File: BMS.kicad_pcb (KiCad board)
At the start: 2 copper layers, 44 parts, among them J28 OLED, SW14 SW_DIP_x01, SW15 SW_DIP_x01, SW16 SW_DIP_x01, U10 ISO1050DUB, U2 TSR_1-2450, U4 Teensy4.1, U6 TBA1-0511E, U7 ISO1050DUB, U8 ISO1050DUB, U9 ISO7221C

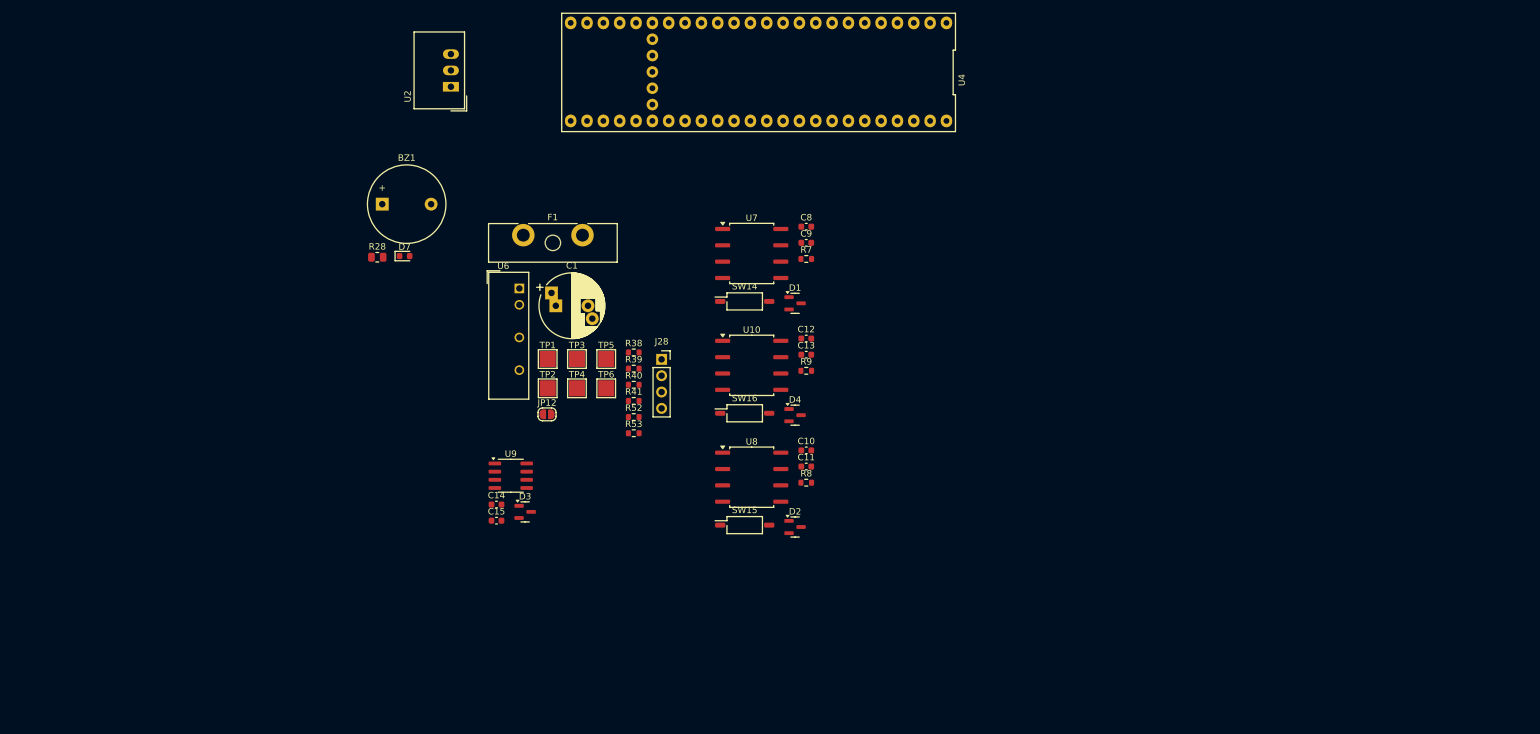
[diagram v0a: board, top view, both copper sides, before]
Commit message: Connectors, high side circuits added, layout progressed
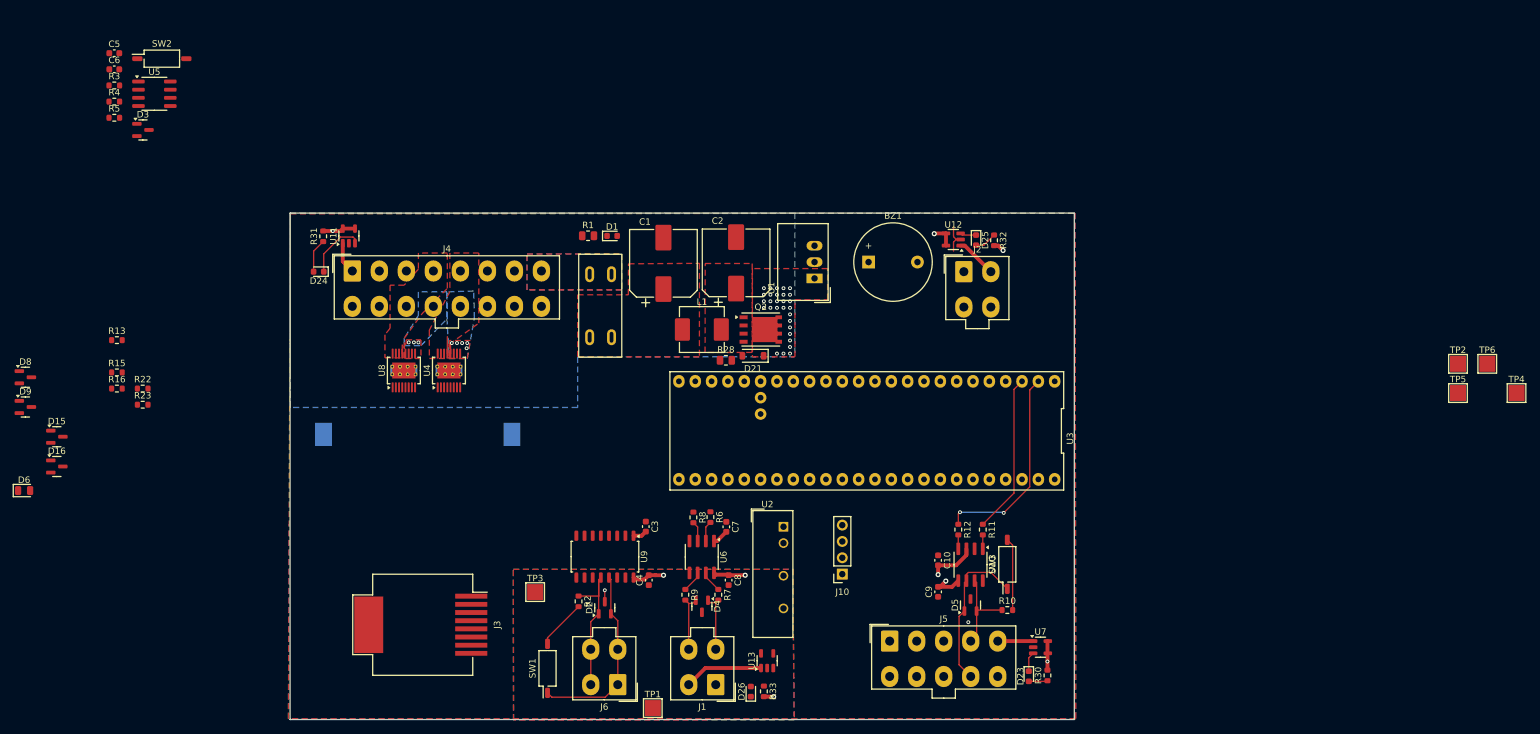
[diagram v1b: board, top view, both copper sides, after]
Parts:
- removed C11, C12, C13: 1uF, Capacitor_SMD:C_0603_1608Metric
- removed the D2 at (155.0, 117.9)
- removed the D4 at (155.0, 100.5)
- removed JP12: SolderJumper_2_Open, Jumper:SolderJumper-2_P1.3mm_Open_RoundedPad1.0x1.5mm
- removed R38, R39, R40, R41, R52, R53: 330R, Resistor_SMD:R_0603_1608Metric
- removed SW15, SW16: SW_DIP_x01, Button_Switch_SMD:SW_DIP_SPSTx01_Slide_Copal_CHS-01B_W7.62mm_P1.27mm
- added BT1: Battery_Cell, Battery:BatteryHolder_Keystone_1060_1x2032, B.Cu at (96.3, 103.5)
- added C2: 470uF, Capacitor_SMD:CP_Elec_10x10, F.Cu at (145.8, 76.8)
- added C5: 1uF, Capacitor_SMD:C_0603_1608Metric, F.Cu at (49.1, 44.2)
- added C6: 1uF, Capacitor_SMD:C_0603_1608Metric, F.Cu at (49.1, 46.7)
- added C9: 1uF, Capacitor_SMD:C_0603_1608Metric, F.Cu at (177.2, 128.0)
- added D15: BAT54S, Package_TO_SOT_SMD:SOT-23, F.Cu at (40.2, 103.9)
- added D16: BAT54S, Package_TO_SOT_SMD:SOT-23, F.Cu at (40.2, 108.5)
- added D21: 10V, Diode_SMD:D_SOD-123, F.Cu at (148.4, 91.3)
- added D23: LED_RED, LED_SMD:LED_0603_1608Metric, F.Cu at (191.3, 141.1)
- added D24: LED_RED, LED_SMD:LED_0603_1608Metric, F.Cu at (80.9, 78.2)
- added D25: LED_RED, LED_SMD:LED_0603_1608Metric, F.Cu at (183.1, 73.3)
- added D26: LED_RED, LED_SMD:LED_0603_1608Metric, F.Cu at (148.1, 143.5)
- added D3: PESD1CAN, Package_TO_SOT_SMD:SOT-23, F.Cu at (53.6, 56.2)
- added D5: PESD1CAN, Package_TO_SOT_SMD:SOT-23, F.Cu at (182.2, 130.0)
- added D6: D, Diode_SMD:D_0805_2012Metric, F.Cu at (35.1, 112.2)
- added D8: BAT54S, Package_TO_SOT_SMD:SOT-23, F.Cu at (35.3, 94.6)
- added D9: BAT54S, Package_TO_SOT_SMD:SOT-23, F.Cu at (35.3, 99.2)
- added J1: Conn_02x02_Counter_Clockwise, Connector_Molex:Molex_Mini-Fit_Jr_5566-04A_2x02_P4.20mm_Vertical, F.Cu at (142.6, 142.4)
- added J2: Conn_02x02_Counter_Clockwise, Connector_Molex:Molex_Mini-Fit_Jr_5566-04A_2x02_P4.20mm_Vertical, F.Cu at (181.2, 78.2)
- added J3: RJ45, Connector_RJ:RJ45_Molex_0855135013_Vertical, F.Cu at (96.8, 133.1)
- added J4: Conn_02x08_Top_Bottom, Connector_Molex:Molex_Mini-Fit_Jr_5566-16A_2x08_P4.20mm_Vertical, F.Cu at (86.1, 78.1)
- added J5: Conn_02x05_Top_Bottom, Connector_Molex:Molex_Mini-Fit_Jr_5566-10A_2x05_P4.20mm_Vertical, F.Cu at (169.7, 135.6)
- added J6: Conn_02x02_Counter_Clockwise, Connector_Molex:Molex_Mini-Fit_Jr_5566-04A_2x02_P4.20mm_Vertical, F.Cu at (127.4, 142.4)
- added L1: 1.5uH, Inductor_SMD:L_Changjiang_FXL0618, F.Cu at (140.5, 87.2)
- added Q2: SIRA00DP-T1-GE3, Package_SO:PowerPAK_SO-8_Single, F.Cu at (149.6, 87.2)
- added R10: 120, Resistor_SMD:R_0603_1608Metric, F.Cu at (188.0, 130.8)
- added R11: 330R, Resistor_SMD:R_0603_1608Metric, F.Cu at (184.2, 118.3)
- added R12: 330R, Resistor_SMD:R_0603_1608Metric, F.Cu at (180.3, 118.3)
- added R13: 4.7k, Resistor_SMD:R_0603_1608Metric, F.Cu at (49.5, 88.8)
- added R15: 15k, Resistor_SMD:R_0603_1608Metric, F.Cu at (49.5, 93.9)
- added R16: 15k, Resistor_SMD:R_0603_1608Metric, F.Cu at (49.5, 96.4)
- added R22: 15k, Resistor_SMD:R_0603_1608Metric, F.Cu at (53.5, 96.4)
- added R23: 15k, Resistor_SMD:R_0603_1608Metric, F.Cu at (53.5, 98.9)
- added R28: 10k, Resistor_SMD:R_0805_2012Metric, F.Cu at (144.2, 92.0)
- added R3: 120, Resistor_SMD:R_0603_1608Metric, F.Cu at (49.1, 49.3)
- added R30: 3.3k, Resistor_SMD:R_0603_1608Metric, F.Cu at (194.2, 141.0)
- added R31: 3.3k, Resistor_SMD:R_0603_1608Metric, F.Cu at (81.6, 72.7)
- added R32: 3.3k, Resistor_SMD:R_0603_1608Metric, F.Cu at (185.9, 73.3)
- added R33: 3.3k, Resistor_SMD:R_0603_1608Metric, F.Cu at (150.1, 143.4)
- added R4: 330R, Resistor_SMD:R_0603_1608Metric, F.Cu at (49.1, 51.8)
- added R5: 330R, Resistor_SMD:R_0603_1608Metric, F.Cu at (49.1, 54.3)
- added R6: 330R, Resistor_SMD:R_0603_1608Metric, F.Cu at (141.8, 116.4)
- added R7: 330R, Resistor_SMD:R_0603_1608Metric, F.Cu at (143.0, 128.4)
- added SW2: SW_DIP_x01, Button_Switch_SMD:SW_DIP_SPSTx01_Slide_Copal_CHS-01B_W7.62mm_P1.27mm, F.Cu at (56.5, 45.1)
- added SW3: SW_DIP_x01, Button_Switch_SMD:SW_DIP_SPSTx01_Slide_Copal_CHS-01B_W7.62mm_P1.27mm, F.Cu at (188.0, 123.7)
- added U11: TPS2051CDBV, Package_TO_SOT_SMD:SOT-23-5, F.Cu at (85.6, 72.6)
- added U12: TPS2051CDBV, Package_TO_SOT_SMD:SOT-23-5, F.Cu at (179.6, 73.2)
- added U13: TPS2051CDBV, Package_TO_SOT_SMD:SOT-23-5, F.Cu at (150.6, 138.7)
- added U4: VND7050AJTR, Package_SO:PowerSSO-16-1EP_3.9x4.9mm_P0.5mm_EP2.5x3.61mm_ThermalVias, F.Cu at (101.2, 93.6)
- added U5: TJA1051T/3/1J, Package_SO:SOIC-8_3.9x4.9mm_P1.27mm, F.Cu at (55.4, 50.5)
- added U9: ISO1050DWR, Package_SO:SOP-16_4.55x10.3mm_P1.27mm, F.Cu at (125.4, 122.5)
- C1: value 1000uf 50V -> 470uF; footprint Capacitor_THT:CP_Radial_D10.0mm_P5.00mm_P7.50mm -> Capacitor_SMD:CP_Elec_10x10
- F1: value 20A Fuse -> Mini Blade Fuse (10A); footprint Fuse:Fuseholder_Blade_ATO_Littelfuse_Pudenz_2_Pin -> user:XFCN XF-508P-B-B
- R8, R9: value 120 -> 330R
- U1: renamed from U2; value TSR_1-2450 -> K7805M-1000R3
- U10: value ISO1050DUB -> TJA1051T/3/1J; footprint Package_SO:SOP-8_6.62x9.15mm_P2.54mm -> Package_SO:SOIC-8_3.9x4.9mm_P1.27mm
- U2: renamed from U6; value TBA1-0511E -> B0505S-3WR2
- U6: renamed from U9; value ISO7221C -> ISO7331C
- U7: value ISO1050DUB -> TPS2051CDBV; footprint Package_SO:SOP-8_6.62x9.15mm_P2.54mm -> Package_TO_SOT_SMD:SOT-23-5
- U8: value ISO1050DUB -> VND7050AJTR; footprint Package_SO:SOP-8_6.62x9.15mm_P2.54mm -> Package_SO:PowerSSO-16-1EP_3.9x4.9mm_P0.5mm_EP2.5x3.61mm_ThermalVias
- moved TP2 141.5 mm to (258.0, 92.5)
- moved TP4 141.5 mm to (267.1, 97.1)
- moved TP5 141.5 mm to (258.0, 97.1)
- moved TP6 141.5 mm to (262.6, 92.5)
- moved BZ1 76.1 mm to (166.4, 76.7)
- moved U7 75.9 mm to (193.1, 136.6)
- moved SW1 64.8 mm to (116.5, 139.9), turned to 90 degrees
- moved R2 63.9 mm to (121.3, 129.5), turned to -90 degrees
- moved U1 63.9 mm to (158.0, 79.2)
- moved U3 58.2 mm to (166.1, 104.1)
- moved C4 57.9 mm to (132.2, 126.2), turned to 90 degrees
- moved U8 56.6 mm to (94.1, 93.6), turned to 90 degrees
- moved D2 55.8 mm to (125.4, 130.5), turned to 90 degrees
- moved U2 55.3 mm to (153.2, 117.9)
- moved TP1 54.7 mm to (132.8, 146.1)
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- renumbered C8 to C3, C9 to C4, C14 to C7, C15 to C8, D7 to D1, D1 to D2, D3 to D4, J28 to J10, R28 to R1, R7 to R2, SW14 to SW1, TP5 to TP1, TP1 to TP2, TP4 to TP3, TP6 to TP4, TP2 to TP5, TP3 to TP6, U4 to U3
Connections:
- net /RAW_INPUT renamed /12V_INPUT
- BZ1 pad 2: +12V -> Net-(BZ1--)
- C1 pad 1: +12V -> Net-(BZ1--)
- C10 pad 2: +3.3V -> +5V
- D1 pad 1: +12V -> Net-(BZ1--)
- F1 pad 2: +12V -> Net-(BZ1--)
- R2 pad 1: /CAN1_HIGH_ISO -> /CAN1_LOW_ISO
- R8 pad 1: /CAN2_HIGH_ISO -> /SERIAL_TX
- R8 pad 2: Net-(R8-Pad2) -> Net-(U6-INB)
- R9 pad 1: /CAN3_HIGH -> Net-(U6-OUTB)
- R9 pad 2: Net-(R9-Pad2) -> /UART_TX_ISO
- SW1 pad 1: GND_ISO -> /CAN1_HIGH_ISO
- TP1 pad 1: GND -> GND_ISO
- TP4 pad 1: GND_ISO -> GND
- U10 pad 1: +3.3V -> Net-(U10-TXD)
- U10 pad 2: /CAN3_RX -> GND
- U10 pad 3: /CAN3_TX -> +5V
- U10 pad 4: GND -> Net-(U10-RXD)
- U10 pad 5: GND -> +3.3V
- U10 pad 6: /CAN3_LOW -> /CAN2_LOW
- U10 pad 7: /CAN3_HIGH -> /CAN2_HIGH
- U10 pad 8: +5V -> unconnected-(U10-Rs-Pad8)
- U3 pad 10: unconnected-(U4-8_TX2_IN1-Pad10) -> /SERIAL_TX
- U3 pad 13: unconnected-(U4-11_MOSI_CTX1-Pad13) -> /HSD_Positive_Contactor_LOGIC
- U3 pad 14: unconnected-(U4-12_MISO_MQSL-Pad14) -> /HSD_PreCharge_Contactor_LOGIC
- U3 pad 15: Net-(JP12-A) -> +3.3V
- U3 pad 2: Net-(U4-0_RX1_CRX2_CS1) -> /CAN2_RX
- U3 pad 22: Net-(U4-30_CRX3) -> /CAN3_RX
- U3 pad 23: Net-(U4-31_CTX3) -> /CAN3_TX
- U3 pad 3: Net-(U4-1_TX1_CTX2_MISO1) -> /CAN2_TX
- U3 pad 42: unconnected-(U4-20_A6_TX5_LRCLK1-Pad42) -> /HSD_Charge_Contactor_LOGIC
- U3 pad 43: unconnected-(U4-21_A7_RX5_BCLK1-Pad43) -> /HSD_Negative_Contactor_LOGIC
- U3 pad 44: Net-(U4-22_A8_CTX1) -> /CAN1_TX
- U3 pad 45: Net-(U4-23_A9_CRX1_MCLK1) -> /CAN1_RX
- U3 pad 49: unconnected-(U4-V_BATT_RTC-Pad49) -> /RTC_BATT_+
- U3 pad 50: unconnected-(U4-3.3V-Pad50) -> +3.3V
- U3 pad 9: unconnected-(U4-7_RX2_OUT1A-Pad9) -> /SERIAL_RX
- U6 pad 2: /UART_RX -> Net-(U6-OUTA)
- U6 pad 3: /UART_TX -> Net-(U6-INB)
- U6 pad 6: /UART_TX_ISO -> Net-(U6-OUTB)
- U6 pad 7: /UART_RX_ISO -> Net-(U6-INA)
- U7 pad 1: +3.3V -> /Overcurrent_Protection/V_{OUT}
- U7 pad 2: /CAN1_RX -> GND
- U7 pad 3: /CAN1_TX -> Net-(D23-K)
- U7 pad 4: GND -> +5V
- U7 pad 5: GND_ISO -> +5V
- U8 pad 1: +3.3V -> Net-(U8-Input_0)
- U8 pad 2: /CAN2_RX -> Net-(U8-~{FaultRST})
- U8 pad 3: /CAN2_TX -> Net-(U8-SEn)
- U8 pad 4: GND -> /High Side Drivers/Driver_Gnd
- U8 pad 5: GND_ISO -> Net-(U8-Select_0)
- U8 pad 6: /CAN2_LOW_ISO -> Net-(U8-Select_1)
- U8 pad 7: /CAN2_HIGH_ISO -> Net-(U8-Multisense)
- U8 pad 8: +5V_ISO -> Net-(U8-Input_1)
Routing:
- net /CAN2_RX: track 0.00 -> 31.5 mm, vias 0 -> 2
- net /CAN1_HIGH_ISO: track 0.00 -> 28.4 mm
- net /CAN2_TX: track 0.00 -> 24.8 mm
- net /CAN2_LOW: track 0.00 -> 24.6 mm
- net +5V: track 0.00 -> 22.6 mm, vias 0 -> 5
- net /CAN1_LOW_ISO: track 0.00 -> 22.5 mm
- net /CAN2_HIGH: track 0.00 -> 13.9 mm
- net /Overcurrent_Protection3/V_{OUT}: track 0.00 -> 12.3 mm
- net +5V_ISO: track 0.00 -> 11.6 mm, vias 0 -> 3
- net Net-(R10-Pad2): track 0.00 -> 11.3 mm
- net +3.3V: track 0.00 -> 9.79 mm, vias 0 -> 1
- net Net-(D24-K): track 0.00 -> 9.50 mm
- net /UART_TX_ISO: track 0.00 -> 9.17 mm
- net /UART_RX_ISO: track 0.00 -> 9.17 mm
- net Net-(R2-Pad2): track 0.00 -> 7.78 mm
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- added copper zone on B.Cu, net +12V
- added copper zone on F.Cu, net +12V
- added copper zone on In2.Cu, net +12V
- added copper zone on In2.Cu, net +3.3V
- added copper zone on In1.Cu, net +5V
- added copper zone on In1.Cu, net +5V_ISO
- added copper zone on In2.Cu, net +5V_ISO
- added copper zone on B.Cu, net /12V_INPUT
- added copper zone on F.Cu, net /12V_INPUT
- added copper zone on In1.Cu, net /12V_INPUT
- added copper zone on In2.Cu, net /12V_INPUT
- added copper zone on B.Cu, net /OUT1_HSD_PWR
- added copper zone on F.Cu, net /OUT1_HSD_PWR
- added copper zone on In2.Cu, net /OUT1_HSD_PWR
- added copper zone on F.Cu, net /OUT2_HSD_PWR
- added copper zone on B.Cu, net /OUT3_HSD_PWR
- added copper zone on F.Cu, net /OUT3_HSD_PWR
- added copper zone on In2.Cu, net /OUT3_HSD_PWR
- added copper zone on F.Cu, net /OUT4_HSD_PWR
- added copper zone on In1.Cu, net /OUT4_HSD_PWR
- added copper zone on B.Cu, net GND
- added copper zone on F.Cu, net GND
- added copper zone on B.Cu, net GND_ISO
- added copper zone on F.Cu, net GND_ISO
- added copper zone on F.Cu, net Net-(BZ1--)
- added copper zone on F.Cu, net Net-(C2-Pad1)
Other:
- board outline added: 121.9 x 78.7 mm
- copper layers 2 -> 4

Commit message: Added LSD, HSD, Improved Layout
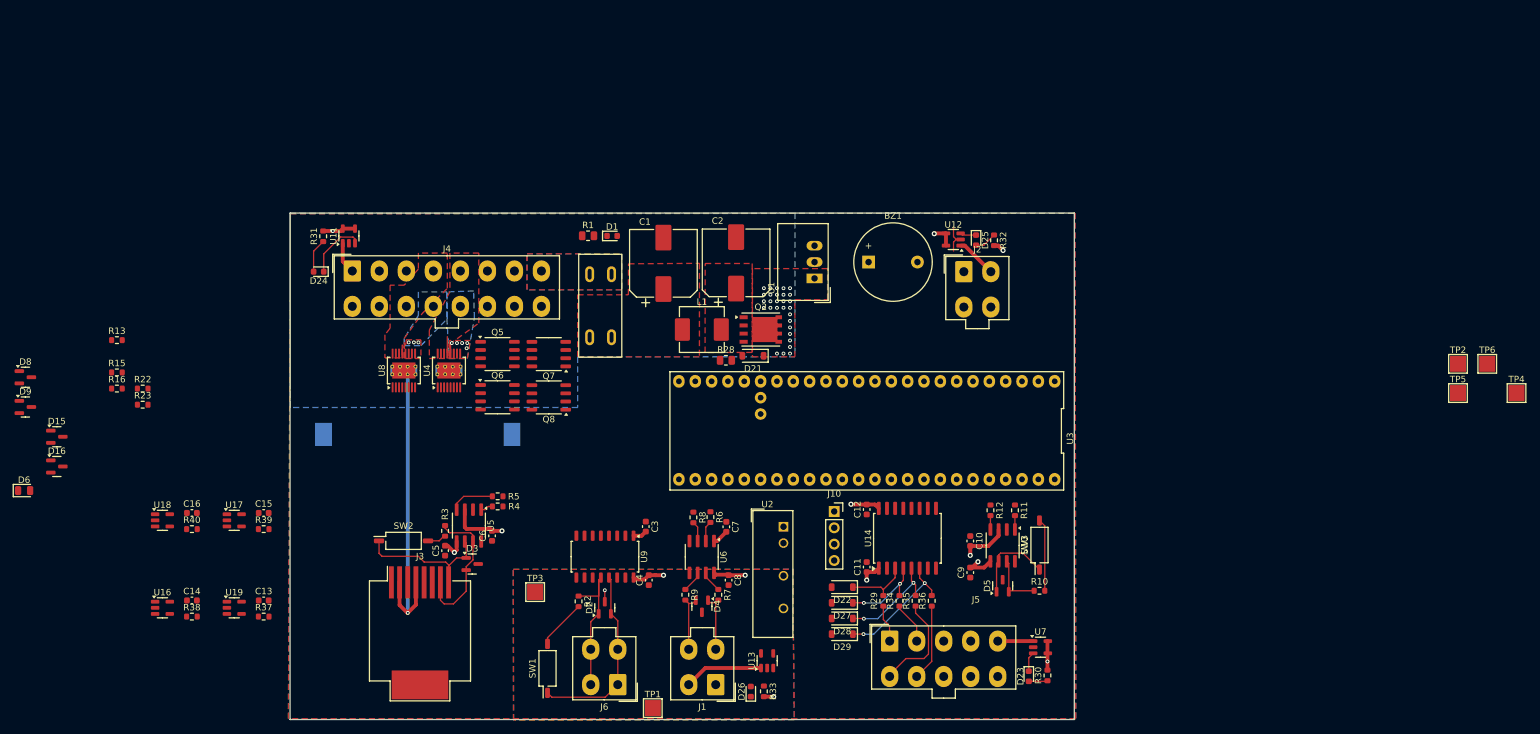
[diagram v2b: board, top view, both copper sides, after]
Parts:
- added C11: 1uF, Capacitor_SMD:C_0603_1608Metric, F.Cu at (166.1, 124.1)
- added C12: 1uF, Capacitor_SMD:C_0603_1608Metric, F.Cu at (166.1, 115.2)
- added C13: 1uF, Capacitor_SMD:C_0603_1608Metric, F.Cu at (72.3, 129.3)
- added C14: 1uF, Capacitor_SMD:C_0603_1608Metric, F.Cu at (61.2, 129.3)
- added C15: 1uF, Capacitor_SMD:C_0603_1608Metric, F.Cu at (72.3, 115.7)
- added C16: 1uF, Capacitor_SMD:C_0603_1608Metric, F.Cu at (61.2, 115.7)
- added D22: 4.7V Zener 500mW, Diode_SMD:D_SOD-123, F.Cu at (162.3, 127.2)
- added D27: 4.7V Zener 500mW, Diode_SMD:D_SOD-123, F.Cu at (162.3, 129.7)
- added D28: 4.7V Zener 500mW, Diode_SMD:D_SOD-123, F.Cu at (162.3, 132.1)
- added D29: 4.7V Zener 500mW, Diode_SMD:D_SOD-123, F.Cu at (162.3, 134.6)
- added Q5: Q_NMOS, Package_SO:SOP-8_3.9x4.9mm_P1.27mm, F.Cu at (108.7, 91.0)
- added Q6: Q_NMOS, Package_SO:SOP-8_3.9x4.9mm_P1.27mm, F.Cu at (108.7, 97.7)
- added Q7: Q_NMOS, Package_SO:SOP-8_3.9x4.9mm_P1.27mm, F.Cu at (116.7, 91.0)
- added Q8: Q_NMOS, Package_SO:SOP-8_3.9x4.9mm_P1.27mm, F.Cu at (116.7, 97.8)
- added R29: 4.7k, Resistor_SMD:R_0603_1608Metric, F.Cu at (168.7, 129.4)
- added R34: 4.7k, Resistor_SMD:R_0603_1608Metric, F.Cu at (171.2, 129.4)
- added R35: 4.7k, Resistor_SMD:R_0603_1608Metric, F.Cu at (173.7, 129.4)
- added R36: 4.7k, Resistor_SMD:R_0603_1608Metric, F.Cu at (176.2, 129.4)
- added R37: 8, Resistor_SMD:R_0603_1608Metric, F.Cu at (72.3, 131.8)
- added R38: 8, Resistor_SMD:R_0603_1608Metric, F.Cu at (61.2, 131.8)
- added R39: 8, Resistor_SMD:R_0603_1608Metric, F.Cu at (72.3, 118.2)
- added R40: 8, Resistor_SMD:R_0603_1608Metric, F.Cu at (61.2, 118.2)
- added U14: CA-IS3740, Package_SO:SOIC-16W_7.5x10.3mm_P1.27mm, F.Cu at (172.4, 119.7)
- added U16: DGD0211CWT-7, Package_TO_SOT_SMD:SOT-23-5, F.Cu at (56.6, 130.5)
- added U17: DGD0211CWT-7, Package_TO_SOT_SMD:SOT-23-5, F.Cu at (67.8, 116.9)
- added U18: DGD0211CWT-7, Package_TO_SOT_SMD:SOT-23-5, F.Cu at (56.6, 116.9)
- added U19: DGD0211CWT-7, Package_TO_SOT_SMD:SOT-23-5, F.Cu at (67.8, 130.5)
- moved C6 93.3 mm to (107.8, 119.3), turned to 90 degrees
- moved C5 92.9 mm to (100.5, 121.6), turned to 90 degrees
- moved R4 86.7 mm to (108.7, 114.7), turned to 180 degrees
- moved R3 86.3 mm to (100.5, 118.5), turned to -90 degrees
- moved D3 84.7 mm to (104.8, 123.7)
- moved SW2 83.9 mm to (94.1, 120.0)
- moved R5 83.8 mm to (108.7, 113.1), turned to 180 degrees
- moved U5 83.1 mm to (104.3, 117.7), turned to -90 degrees
- moved J10 9.82 mm to (161.1, 115.5), turned to 0 degrees
- moved C10 5.83 mm to (182.2, 120.1)
- moved C9 5.83 mm to (182.2, 125.0)
- moved D5 5.83 mm to (187.2, 127.0)
- moved R10 5.83 mm to (193.0, 127.8)
- moved R11 5.83 mm to (189.2, 115.3)
- moved R12 5.83 mm to (185.3, 115.3)
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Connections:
- net /HSD_Charge_Contactor_LOGIC renamed /OUT3_HSD_LOGIC
- net /HSD_Negative_Contactor_LOGIC renamed /OUT4_HSD_LOGIC
- net /HSD_Positive_Contactor_LOGIC renamed /OUT1_HSD_LOGIC
- net /HSD_PreCharge_Contactor_LOGIC renamed /OUT2_HSD_LOGIC
- U3 pad 4: unconnected-(U3-2_OUT2-Pad4) -> /OUT5_LSD_LOGIC
- U3 pad 5: unconnected-(U3-3_LRCLK2-Pad5) -> /OUT6_LSD_LOGIC
- U3 pad 7: unconnected-(U3-5_IN2-Pad7) -> /OUT7_LSD_LOGIC
- U3 pad 8: unconnected-(U3-6_OUT1D-Pad8) -> /OUT8_LSD_LOGIC
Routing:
- net +12V: track 0.00 -> 48.5 mm, vias 29 -> 30
- net /CAN2_RX: track 31.5 -> 0.00 mm, vias 2 -> 0
- net /CAN2_TX: track 24.8 -> 0.00 mm
- net /CAN3_LOW: track 0.00 -> 23.8 mm
- net /CAN3_HIGH: track 0.00 -> 22.2 mm
- net Net-(D29-K): track 0.00 -> 19.5 mm, vias 0 -> 2
- net Net-(D28-K): track 0.00 -> 16.3 mm, vias 0 -> 2
- net /In_3: track 0.00 -> 15.9 mm
- net Net-(D27-K): track 0.00 -> 13.1 mm, vias 0 -> 2
- net +5V: track 22.6 -> 34.7 mm, vias 5 -> 7
- net /In_4: track 0.00 -> 11.9 mm
- net /CAN2_LOW: track 24.6 -> 13.4 mm
- net Net-(D22-K): track 0.00 -> 9.90 mm
- net +3.3V: track 9.79 -> 18.1 mm, vias 1 -> 3
- net Net-(U5-RXD): track 0.00 -> 6.98 mm
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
